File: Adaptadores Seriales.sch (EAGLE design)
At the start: 18 parts, among them X13 22-23-2031, X14 22-23-2031, X15 22-23-2031, X16 22-23-2031, X17 22-23-2031, X18 22-23-2031

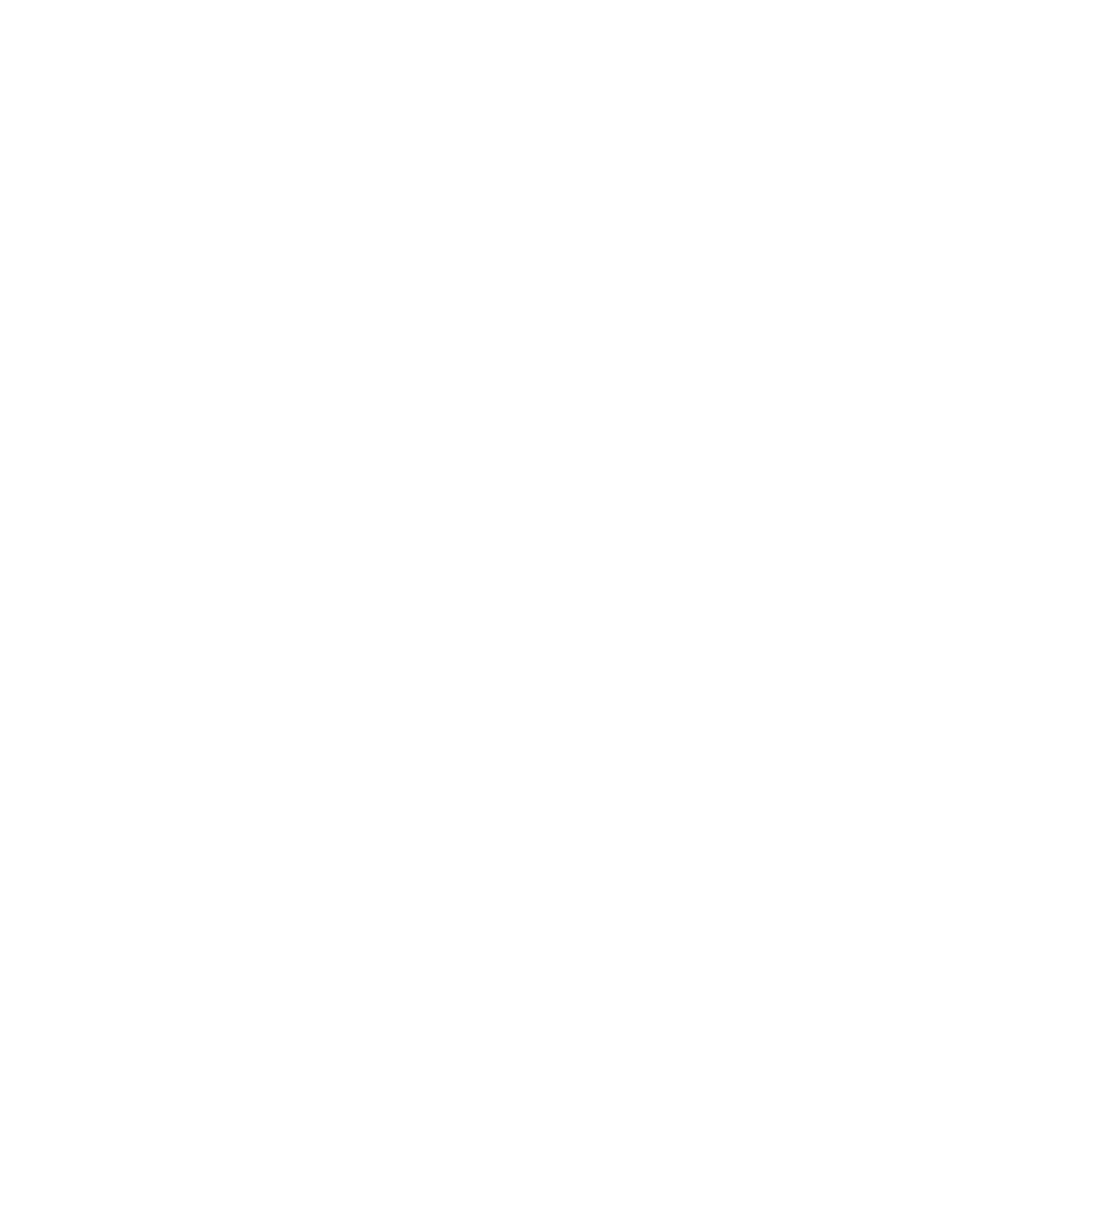
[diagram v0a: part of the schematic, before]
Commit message: Añadido Conversor MAX-232, con pine de 3v3 para Raspberry
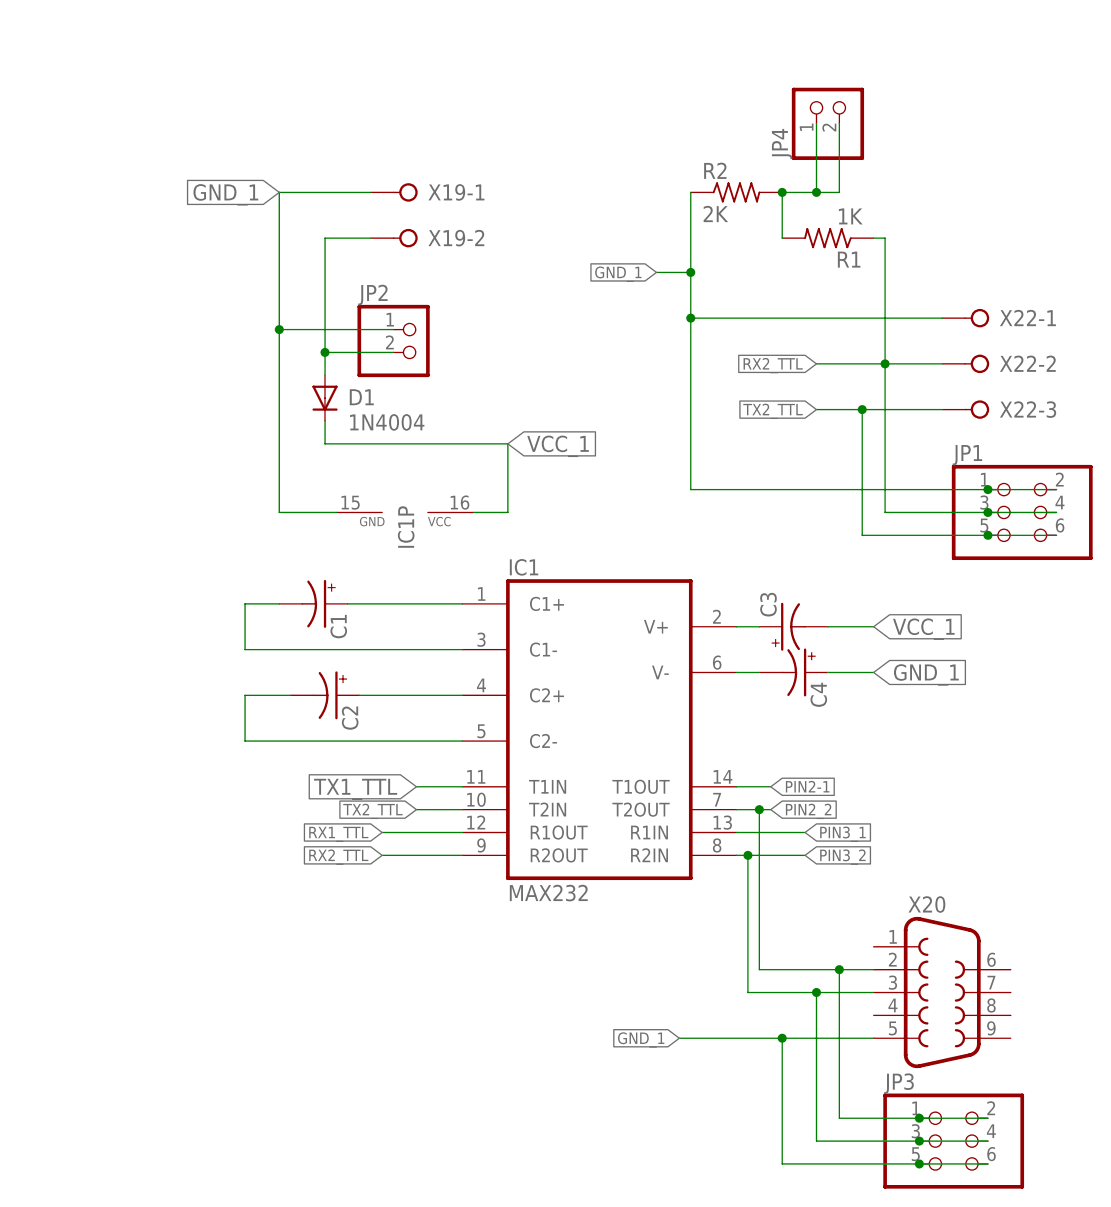
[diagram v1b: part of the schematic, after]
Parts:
- added C1, C2, C3, C4: (no value), SparkFun-Capacitors:10UF-25V-20%(PTH)KIT
- added D1: 1N4004, diode:1N4004
- added IC1: MAX232, maxim:MAX232
- added JP1, JP3: (no value), pinhead:PINHD-2X3
- added JP2, JP4: (no value), pinhead:PINHD-1X2
- added R1: 1K, rcl:R-US_0204/2V
- added R2: 2K, rcl:R-US_0204/2V
- added X19: (no value), con-wago-508:W237-02P
- added X20: (no value), con-subd:F09D
- added X22: (no value), con-wago-508:W237-03P
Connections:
- new net GND_1: C4.+, IC1P.GND, JP1.1, JP1.2, JP2.1, JP3.5, JP3.6, R2.1, X19-1.KL, X20.5, X22-1.KL
- new net N$1: C1.+, IC1G$1.C1+
- new net N$10: C4.-, IC1G$1.V-
- new net N$13: JP4.1, JP4.2, R1.2, R2.2
- new net N$4: C1.-, IC1G$1.C1-
- new net N$6: D1.A, JP2.2, X19-2.KL
- new net N$7: C2.+, IC1G$1.C2+
- new net N$8: C2.-, IC1G$1.C2-
- new net N$9: C3.+, IC1G$1.V+
- new net PIN2-1: IC1G$1.T1OUT
- new net PIN2_2: IC1G$1.T2OUT, JP3.1, JP3.2, X20.2
- new net PIN3_1: IC1G$1.R1IN
- new net PIN3_2: IC1G$1.R2IN, JP3.3, JP3.4, X20.3
- new net RX1_TTL: IC1G$1.R1OUT
- new net RX2_TTL: IC1G$1.R2OUT, JP1.3, JP1.4, R1.1, X22-2.KL
- new net TX1_TTL: IC1G$1.T1IN
- new net TX2_TTL: IC1G$1.T2IN, JP1.5, JP1.6, X22-3.KL
- new net VCC_1: C3.-, D1.C, IC1P.VCC
